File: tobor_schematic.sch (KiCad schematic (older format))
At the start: 9 parts

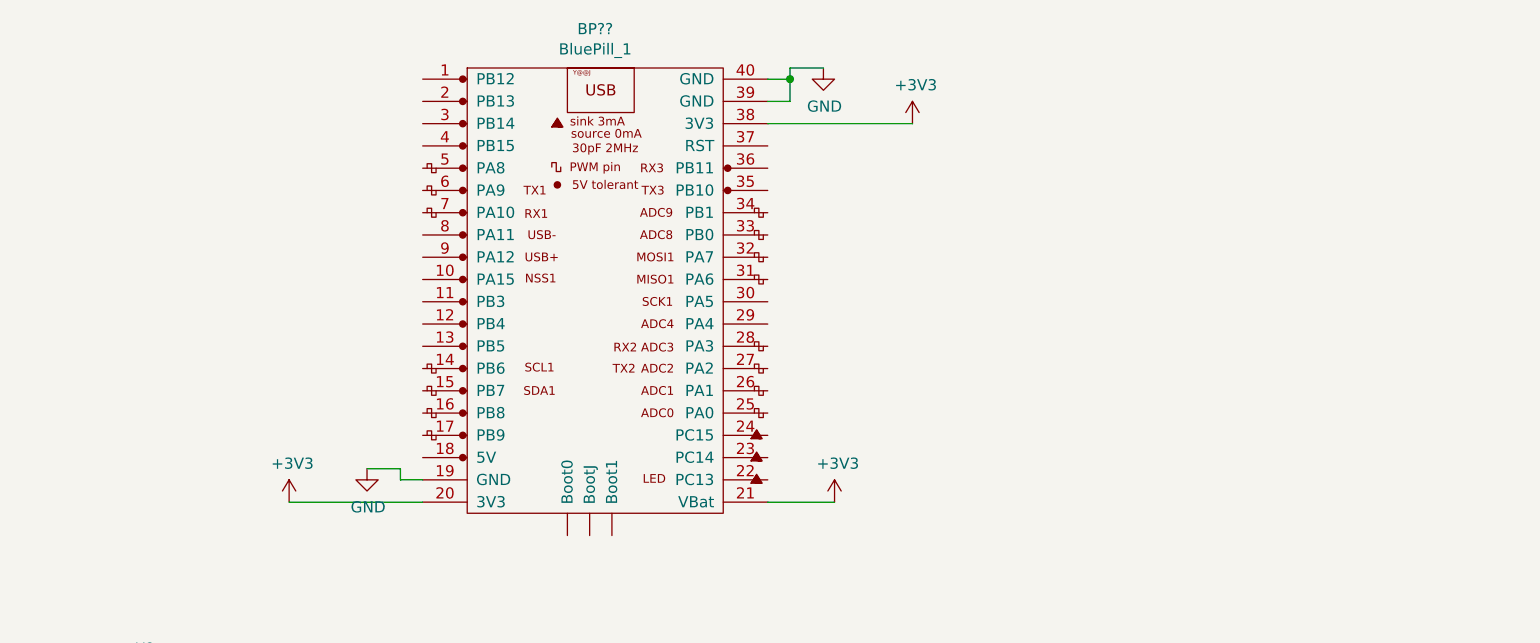
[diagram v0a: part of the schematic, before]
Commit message: Add limit and RST switches
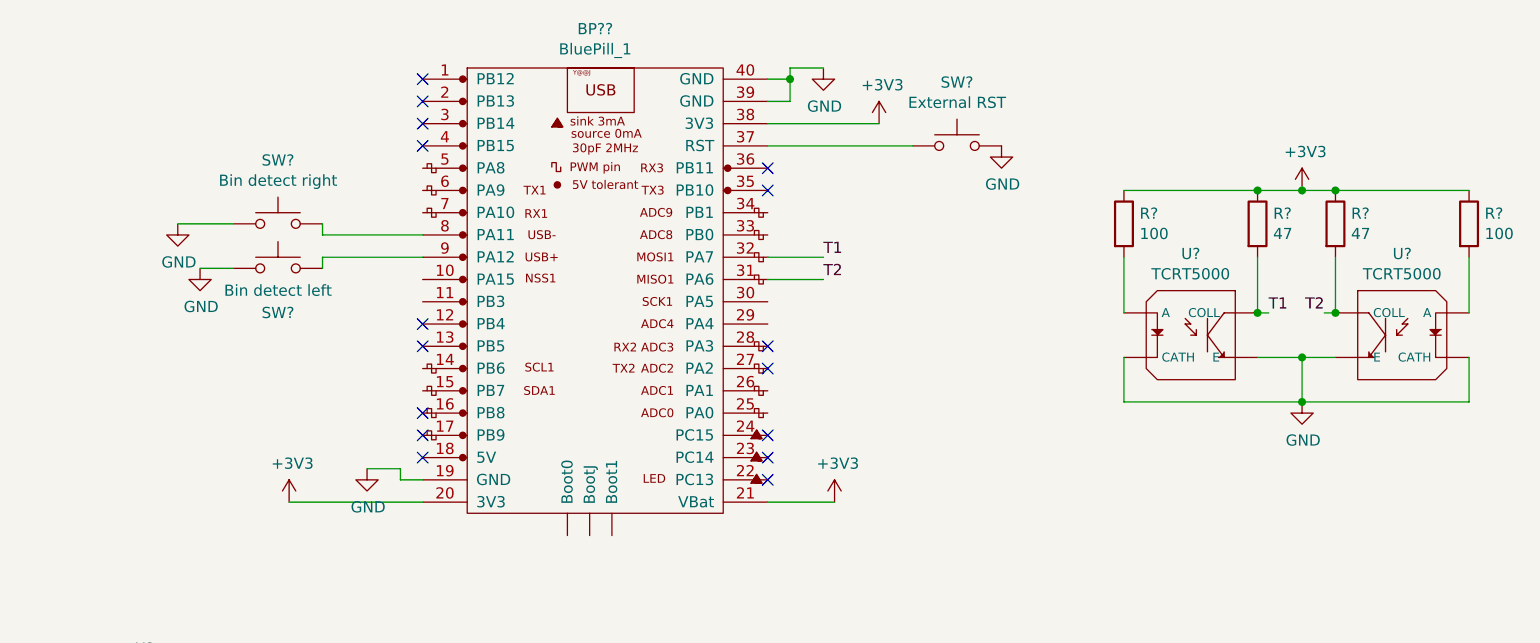
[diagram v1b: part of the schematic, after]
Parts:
- added R? (x2): 100, symbol Device:R
- added R? (x2): 47, symbol Device:R
- added SW?: Bin detect right, symbol Switch:SW_Push
- added SW?: Bin detect left, symbol Switch:SW_Push
- added SW?: External RST, symbol Switch:SW_Push
- added U? (x2): TCRT5000, OPTO_TCRT5000, symbol TCRT5000:TCRT5000
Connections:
- net +3V3: now also R?.1, R?.1, R?.1, R?.1
- net GND: now also SW?.1, SW?.1, SW?.2, U?.CATH, U?.CATH, U?.E, U?.E
- net T2: now reaches BP??.31 (PA6)
- net T2: now also R?.2, U?.C (COLL)
- net T1: now reaches BP??.32 (PA7)
- net T1: now also R?.2, U?.C (COLL)
- net at BP??.37 (RST): now also SW?.1
- net at BP??.8 (PA11): now also SW?.2
- net at BP??.9 (PA12): now also SW?.2
- new net: R?.2, U?.A (x2)
- no-connect marks 0 -> 16

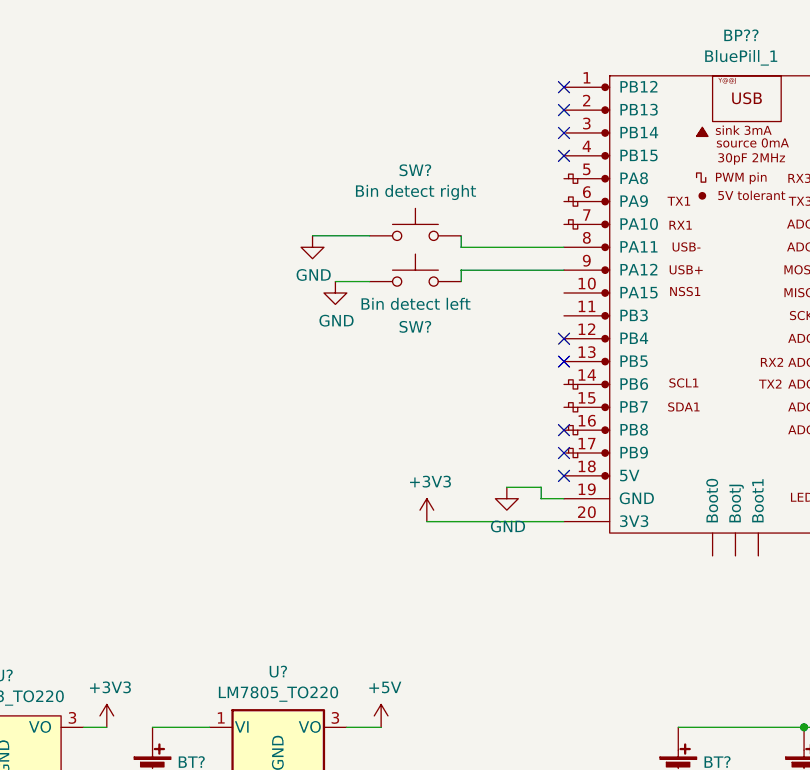
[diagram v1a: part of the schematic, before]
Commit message: Add programming headers
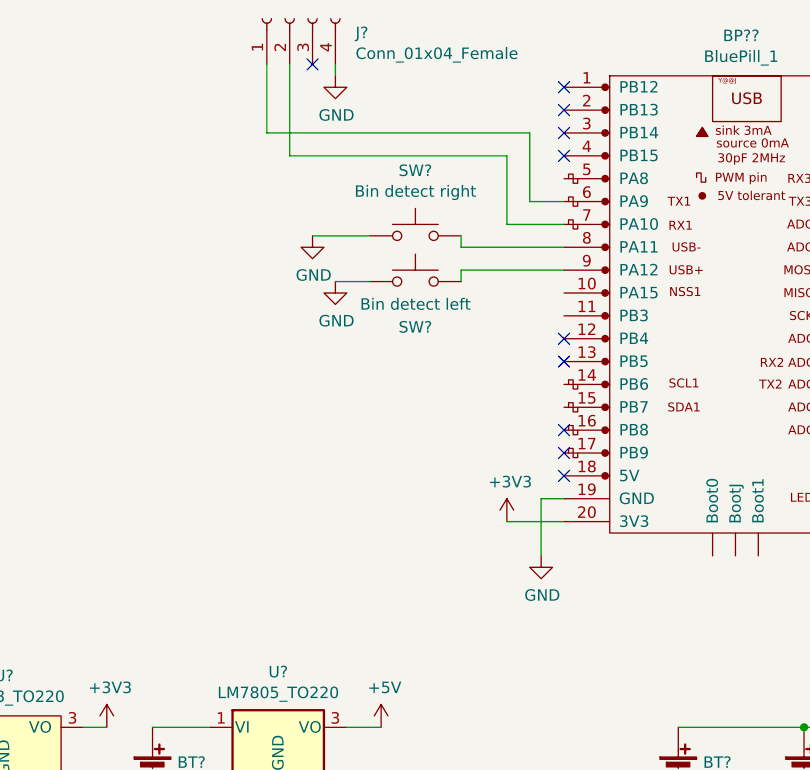
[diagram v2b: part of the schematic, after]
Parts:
- added J?: Conn_01x04_Female, symbol Connector:Conn_01x04_Female
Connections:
- net GND: now also J?.4 (Pin_4)
- net at BP??.6 (PA9): now also J?.1 (Pin_1)
- net at BP??.7 (PA10): now also J?.2 (Pin_2)
- no-connect marks 16 -> 17
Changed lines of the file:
@@
 L power:+3V3 #PWR?
 U 1 1 5EF95DE4
-P 4600 4950
-F 0 "#PWR?" H 4600 4800 50  0001 C CNN
-F 1 "+3V3" H 4615 5123 50  0000 C CNN
-F 2 "" H 4600 4950 50  0001 C CNN
-F 3 "" H 4600 4950 50  0001 C CNN
-	1    4600 4950
-	1    0    0    -1
-$EndComp
-Wire Wire Line
-	4600 4950 5200 4950
+P 4950 4950
+F 0 "#PWR?" H 4950 4800 50  0001 C CNN
+F 1 "+3V3" H 4965 5123 50  0000 C CNN
+F 2 "" H 4950 4950 50  0001 C CNN
+F 3 "" H 4950 4950 50  0001 C CNN
+	1    4950 4950
+	1    0    0    -1
+$EndComp
+Wire Wire Line
+	4950 4950 5200 4950
 $Comp
 L power:GND #PWR?
 U 1 1 5EF96CE8
-P 4950 4800
-F 0 "#PWR?" H 4950 4550 50  0001 C CNN
-F 1 "GND" H 4955 4627 50  0000 C CNN
-F 2 "" H 4950 4800 50  0001 C CNN
-F 3 "" H 4950 4800 50  0001 C CNN
-	1    4950 4800
-	1    0    0    -1
-$EndComp
-Wire Wire Line
-	4950 4800 5100 4800
-Wire Wire Line
-	5100 4800 5100 4850
+P 5100 5100
+F 0 "#PWR?" H 5100 4850 50  0001 C CNN
+F 1 "GND" H 5105 4927 50  0000 C CNN
+F 2 "" H 5100 5100 50  0001 C CNN
+F 3 "" H 5100 5100 50  0001 C CNN
+	1    5100 5100
+	1    0    0    -1
+$EndComp
+Wire Wire Line
+	5100 5100 5100 4850
 Wire Wire Line
 	5100 4850 5200 4850
@@
 	1    0    0    -1
 $EndComp
+$Comp
+L Connector:Conn_01x04_Female J?
+U 1 1 5EFA8BEC
+P 4000 2750
+F 0 "J?" V 3938 2462 50  0000 R CNN
+F 1 "Conn_01x04_Female" V 3847 2462 50  0000 R CNN
+F 2 "" H 4000 2750 50  0001 C CNN
+F 3 "~" H 4000 2750 50  0001 C CNN
+	1    4000 2750
+	0    -1   -1   0
+$EndComp
+Wire Wire Line
+	5200 3650 4950 3650
+Wire Wire Line
+	4950 3650 4950 3350
+Wire Wire Line
+	4950 3350 4000 3350
+Wire Wire Line
+	4000 3350 4000 2950
+Wire Wire Line
+	5200 3550 5050 3550
+Wire Wire Line
+	5050 3550 5050 3250
+Wire Wire Line
+	5050 3250 3900 3250
+Wire Wire Line
+	3900 3250 3900 2950
+NoConn ~ 4100 2950
+$Comp
+L power:GND #PWR?
+U 1 1 5EFB4085
+P 4200 3000
+F 0 "#PWR?" H 4200 2750 50  0001 C CNN
+F 1 "GND" H 4205 2827 50  0000 C CNN
+F 2 "" H 4200 3000 50  0001 C CNN
+F 3 "" H 4200 3000 50  0001 C CNN
+	1    4200 3000
+	1    0    0    -1
+$EndComp
+Wire Wire Line
+	4200 3000 4200 2950
 $EndSCHEMATC
